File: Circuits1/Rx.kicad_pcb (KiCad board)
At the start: 2 copper layers, 43 parts, among them CON1 USB-MINI-B, P1 CONN_3X2, SW1 SW_PUSH, U1 ATMEGA32U4, U2 LD1117, U3 NRF24L01+, X1 QUARTZ, X2 QUARTZ

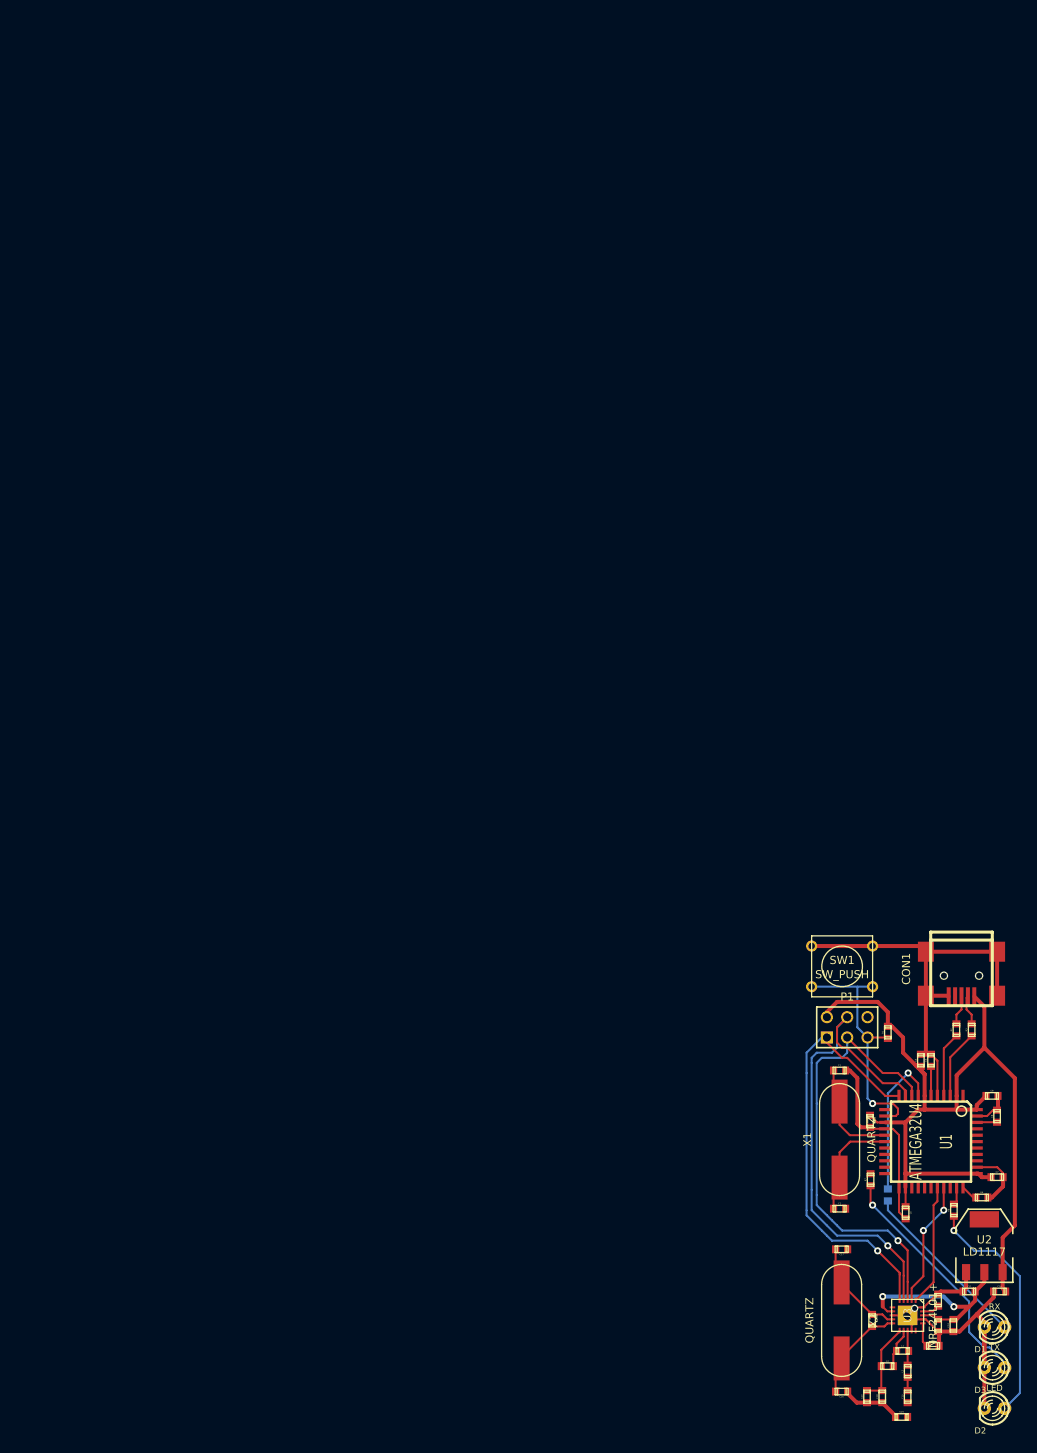
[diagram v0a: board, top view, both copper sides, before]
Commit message: Antenna and Ground Planes
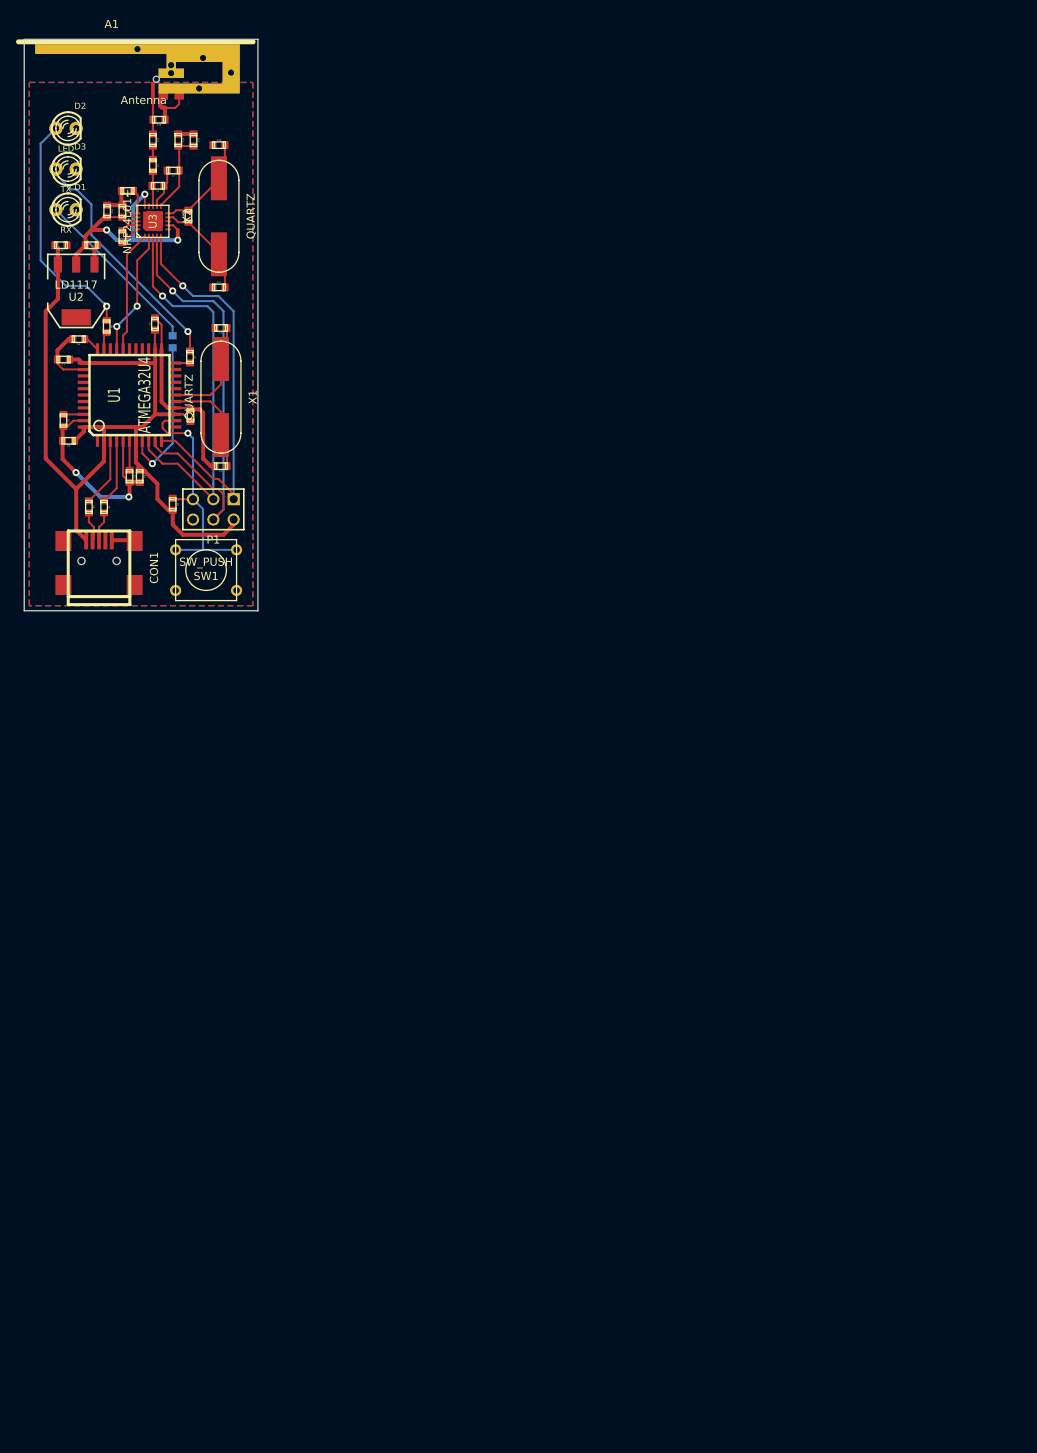
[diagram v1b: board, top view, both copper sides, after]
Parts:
- added A1: Antenna, Antenna, F.Cu at (29.1, 28.2)
- moved D2 197.7 mm to (36.3, 38.8), turned to 0 degrees
- moved D3 189.5 mm to (36.3, 43.8), turned to 0 degrees
- moved C19 186.8 mm to (48.0, 37.7), turned to 180 degrees
- moved C15 183.2 mm to (47.2, 40.2), turned to 270 degrees
- moved D1 181.6 mm to (36.3, 48.9), turned to 0 degrees
- moved C18 180.0 mm to (50.4, 40.2), turned to 270 degrees
- moved C20 178.2 mm to (52.3, 40.2), turned to 270 degrees
- moved L2 177.8 mm to (47.2, 43.4), turned to 270 degrees
- moved R8 176.0 mm to (44.0, 46.6), turned to 180 degrees
- moved C10 175.7 mm to (35.7, 53.4), turned to 180 degrees
- moved C14 174.9 mm to (41.5, 49.1), turned to 270 degrees
- moved C16 174.2 mm to (55.5, 40.9), turned to 0 degrees
- moved L3 174.1 mm to (49.7, 44.0), turned to 180 degrees
- moved L1 172.8 mm to (47.8, 45.9), turned to 180 degrees
- moved C13 172.6 mm to (43.4, 49.1), turned to 270 degrees
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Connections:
- U3 pad : (no net) -> GND
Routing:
- net GND: track 146.6 -> 90.9 mm, vias 0 -> 2
- net 3V3: track 25.8 -> 33.7 mm, vias 2 -> 3
- net /ICSP Header/SCK: track 55.7 -> 50.3 mm
- net ANTENNA: track 0.00 -> 5.42 mm
- net /ICSP Header/MOSI: track 61.5 -> 57.0 mm
- net /ICSP Header/MISO: track 54.1 -> 50.9 mm
- net N-0000012: track 0.00 -> 1.85 mm
- added copper zone on B.Cu, net GND
- added copper zone on F.Cu, net GND
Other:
- board outline added: 29.2 x 71.4 mm
- net class Antenna added: clearance 0.1, trace_width 0.277, via_dia 0.889, via_drill 0.635

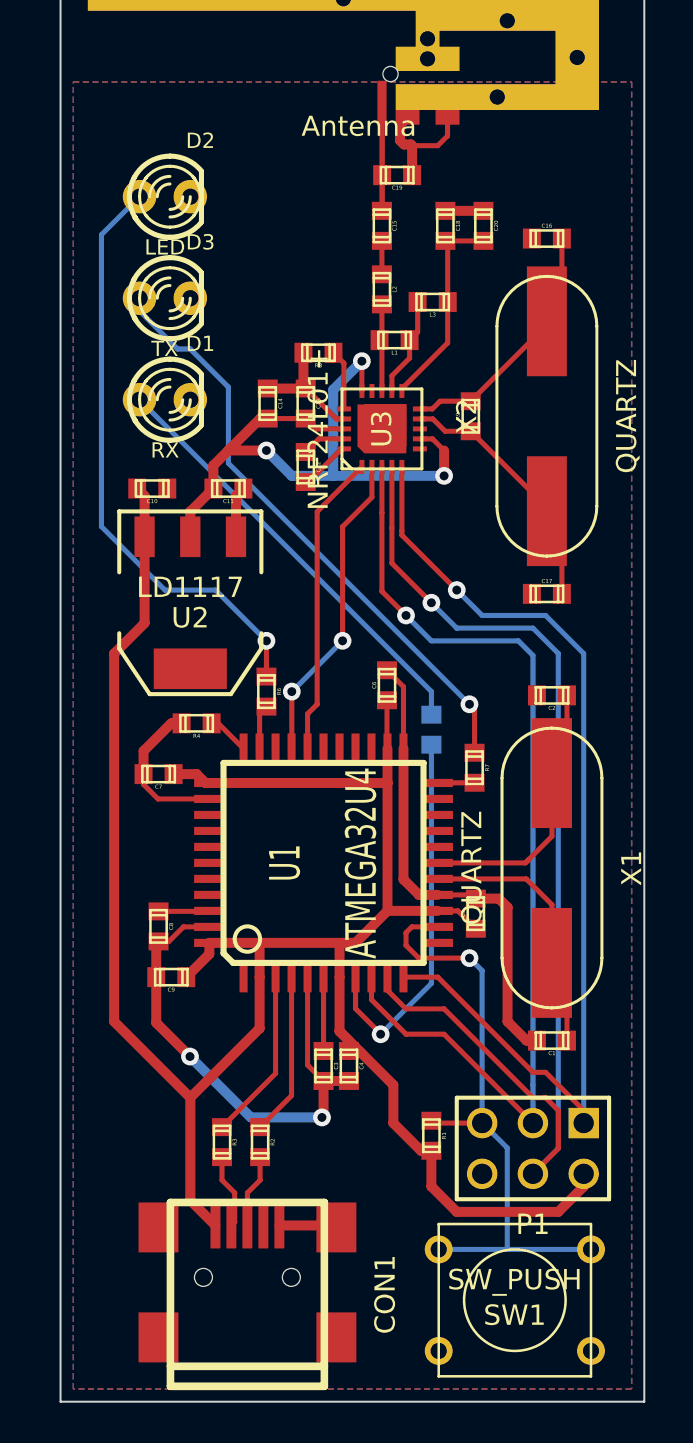
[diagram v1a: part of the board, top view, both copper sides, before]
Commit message: Vias Stitched
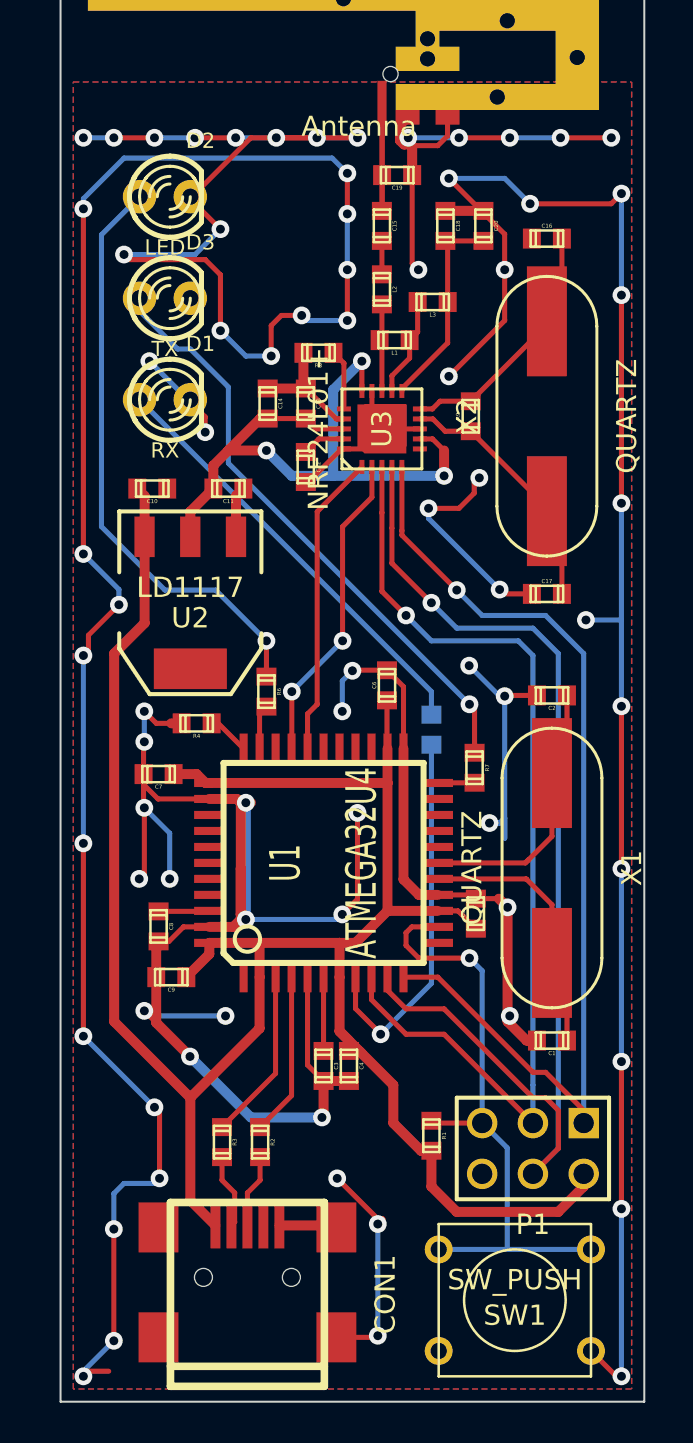
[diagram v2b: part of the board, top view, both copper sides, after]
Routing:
- net GND: track 90.9 -> 430.6 mm, vias 2 -> 75
